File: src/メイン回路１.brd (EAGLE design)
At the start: 22 parts

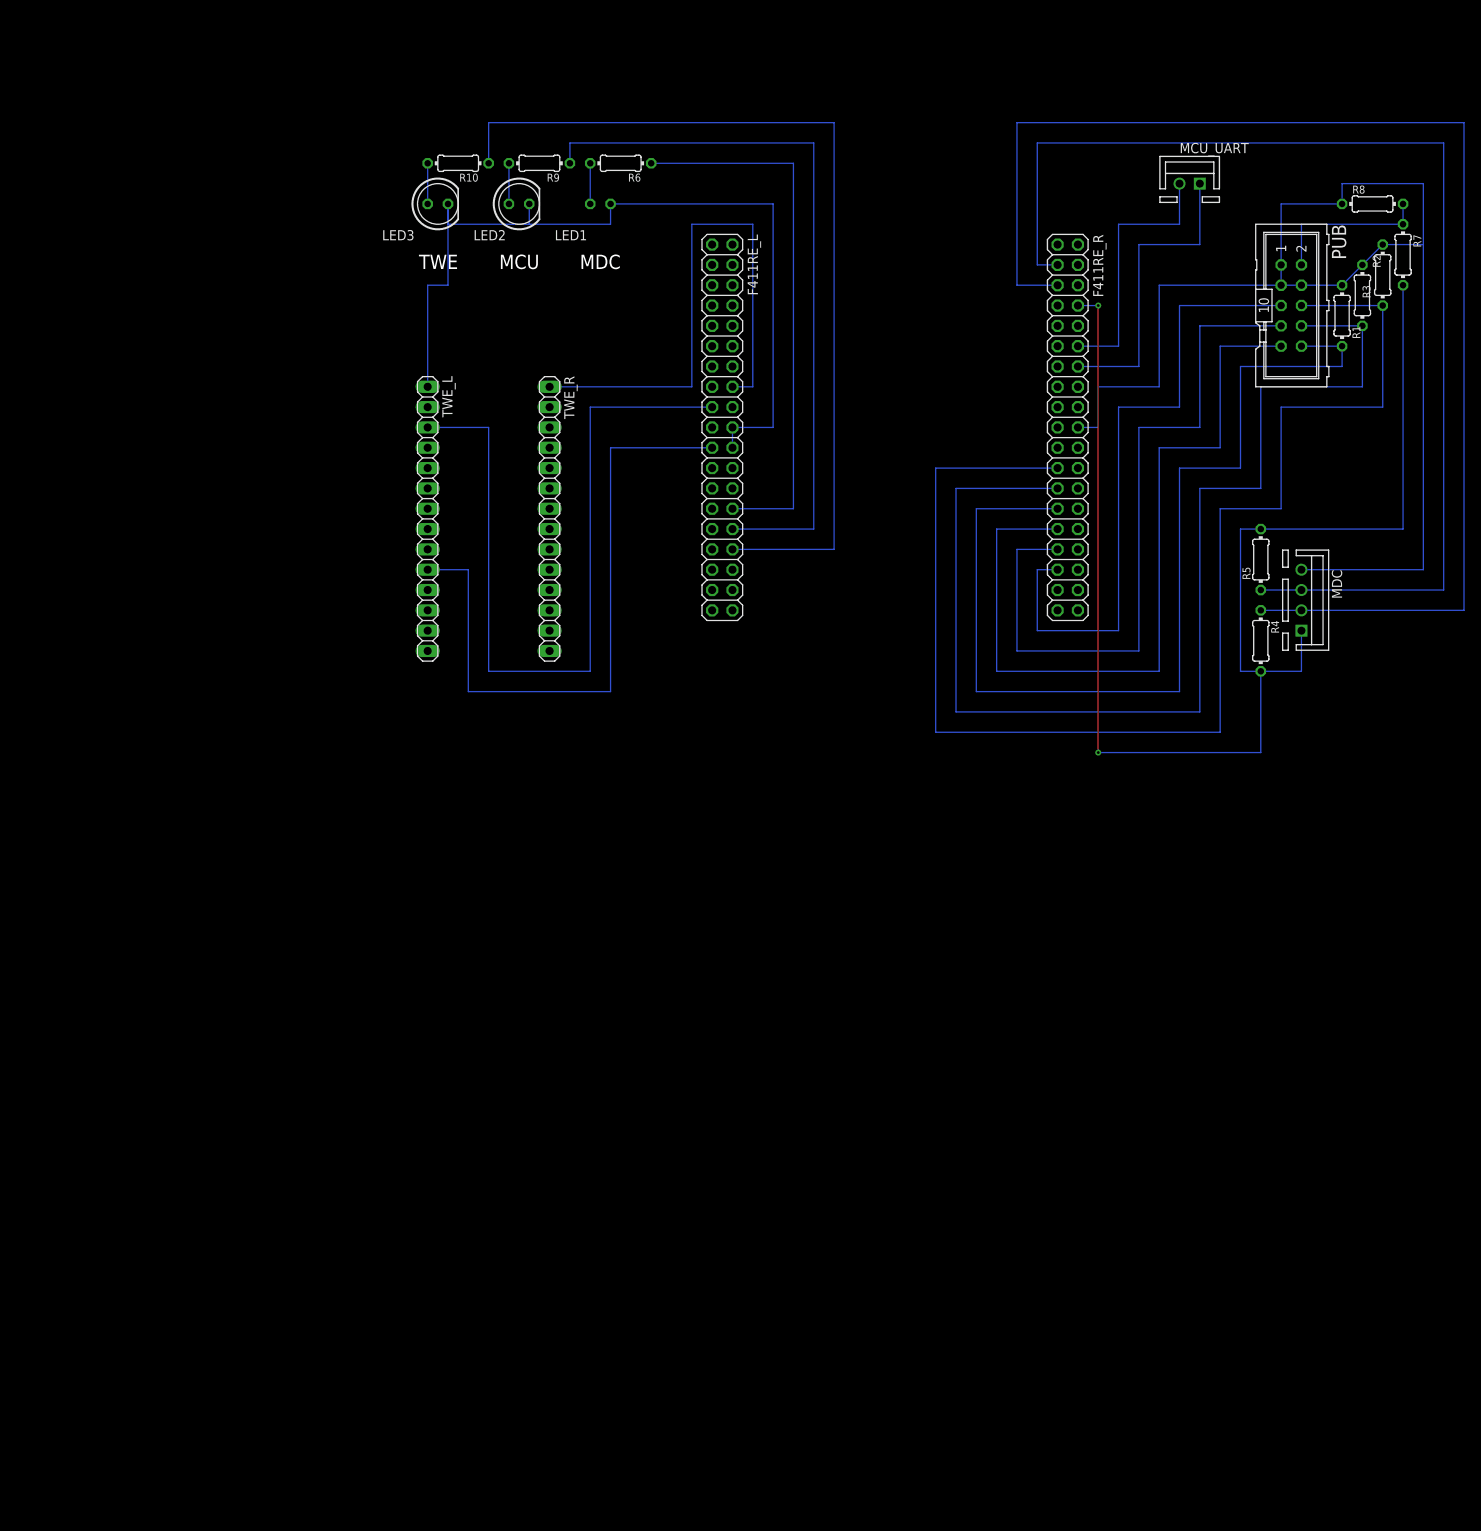
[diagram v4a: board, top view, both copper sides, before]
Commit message: [add]暴走対策回路の追加--ここから--
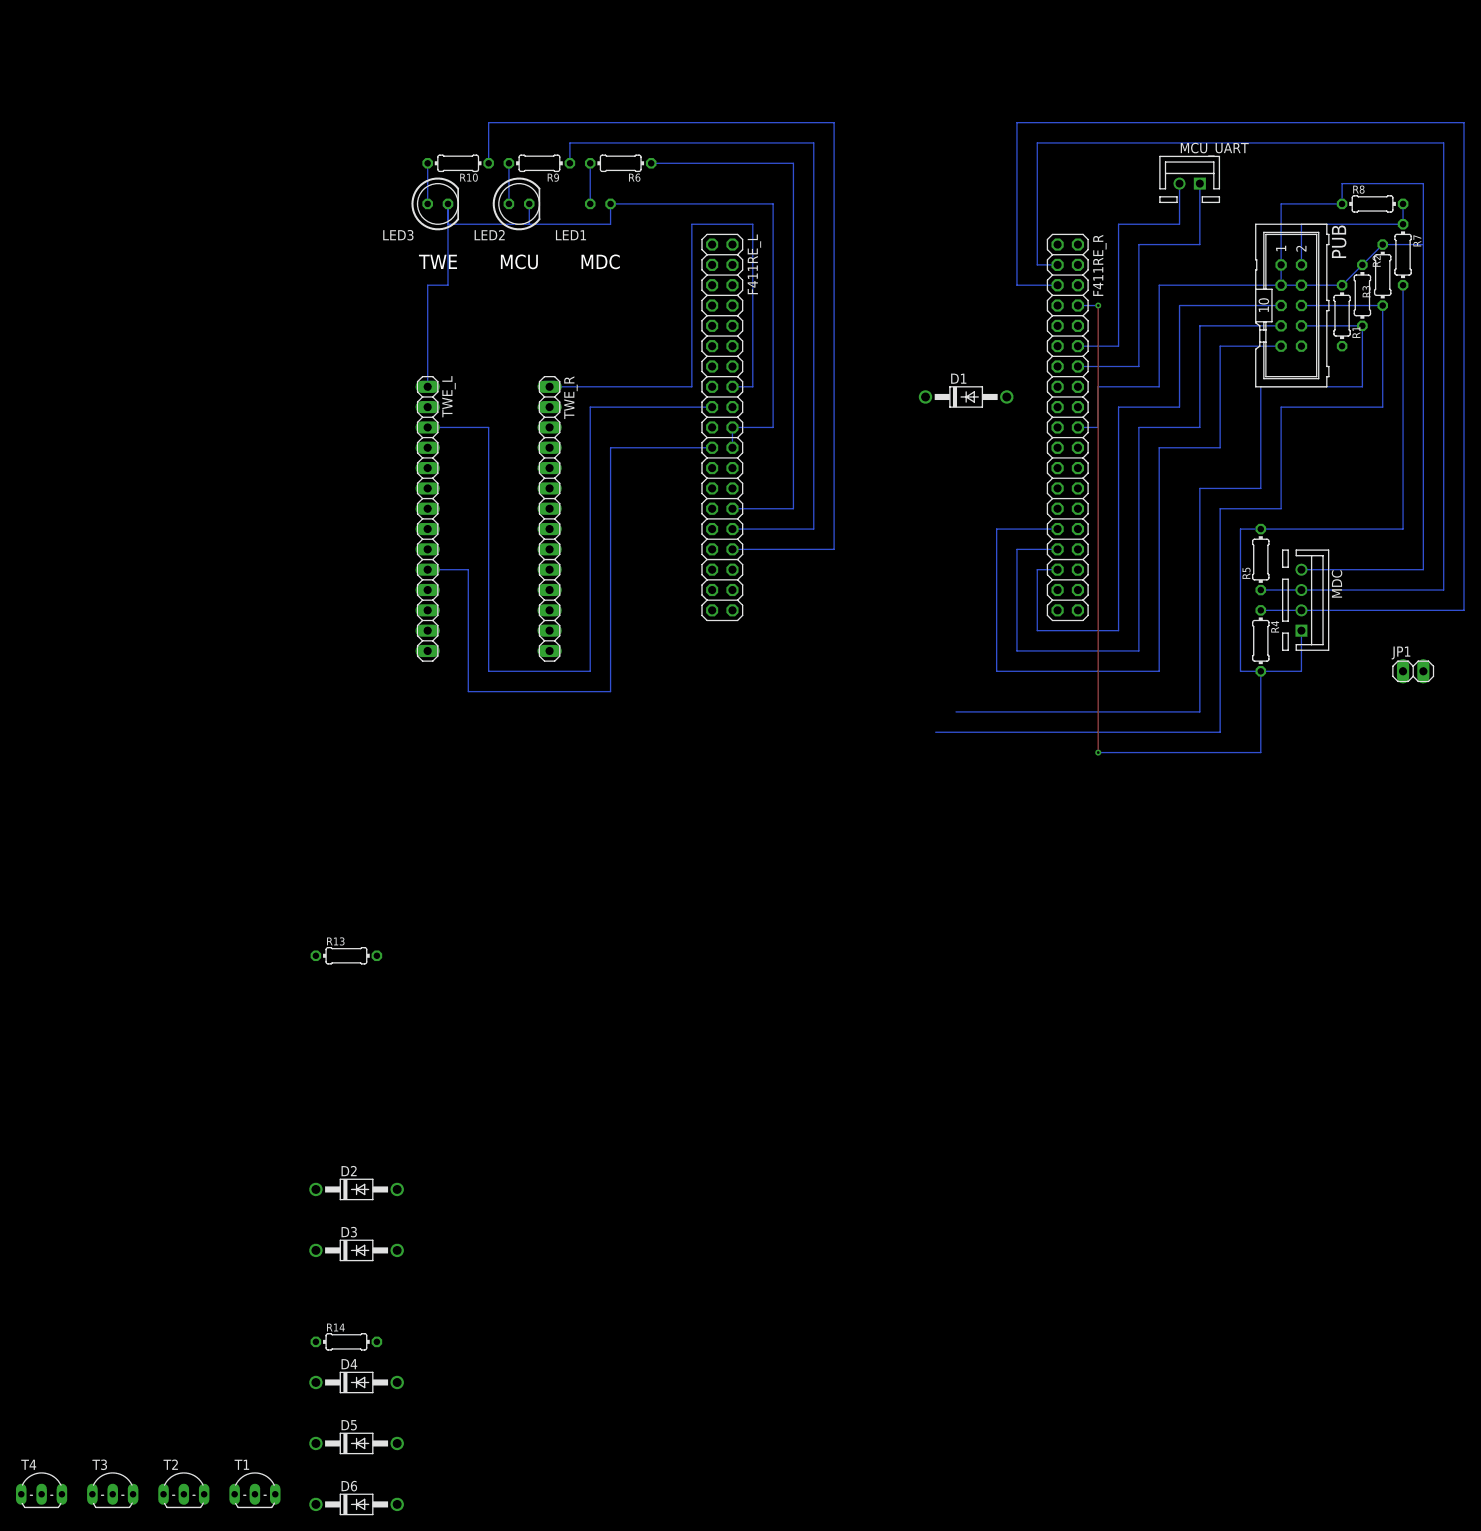
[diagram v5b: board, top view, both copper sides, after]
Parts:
- added D1, D2, D3, D4, D5, D6: 1N4004, diode:DO41-10
- added JP1: (no value), pinhead:1X02
- added R13, R14: 10k, rcl:0204/7
- added T1, T2, T3, T4: 一般的なトランジスタ, 一般的なトランジスタ:TO92-CEB
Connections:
- new net DEBUG: D4.A, D5.A, D6.A, JP1.2, R13.1
- new net N$4: R13.2, T1.B
- new net N$5: D3.C, T2.C
- new net N$6: D2.C, T3.C
- new net N$7: D1.C, T4.C
- new net ZM: R14.1, T1.C, T2.B, T3.B, T4.B
- net DIR1: now also D4.C
- net DIR2: now also D5.C
- net DIR3: now also D6.C
- net GND: now also T1.E
- net PWM1: now also D1.A, T4.E
- net PWM2: now also D2.A, T3.E
- net PWM3: now also D3.A, T2.E
- net U5V: now also JP1.1, R14.2
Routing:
- net PWM1: track 127.0 -> 0.00 mm
- net PWM3: track 167.6 -> 119.4 mm
- net PWM2: track 147.3 -> 106.7 mm

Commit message: [complete]メイン回路1の暴走対策回路の配線完了
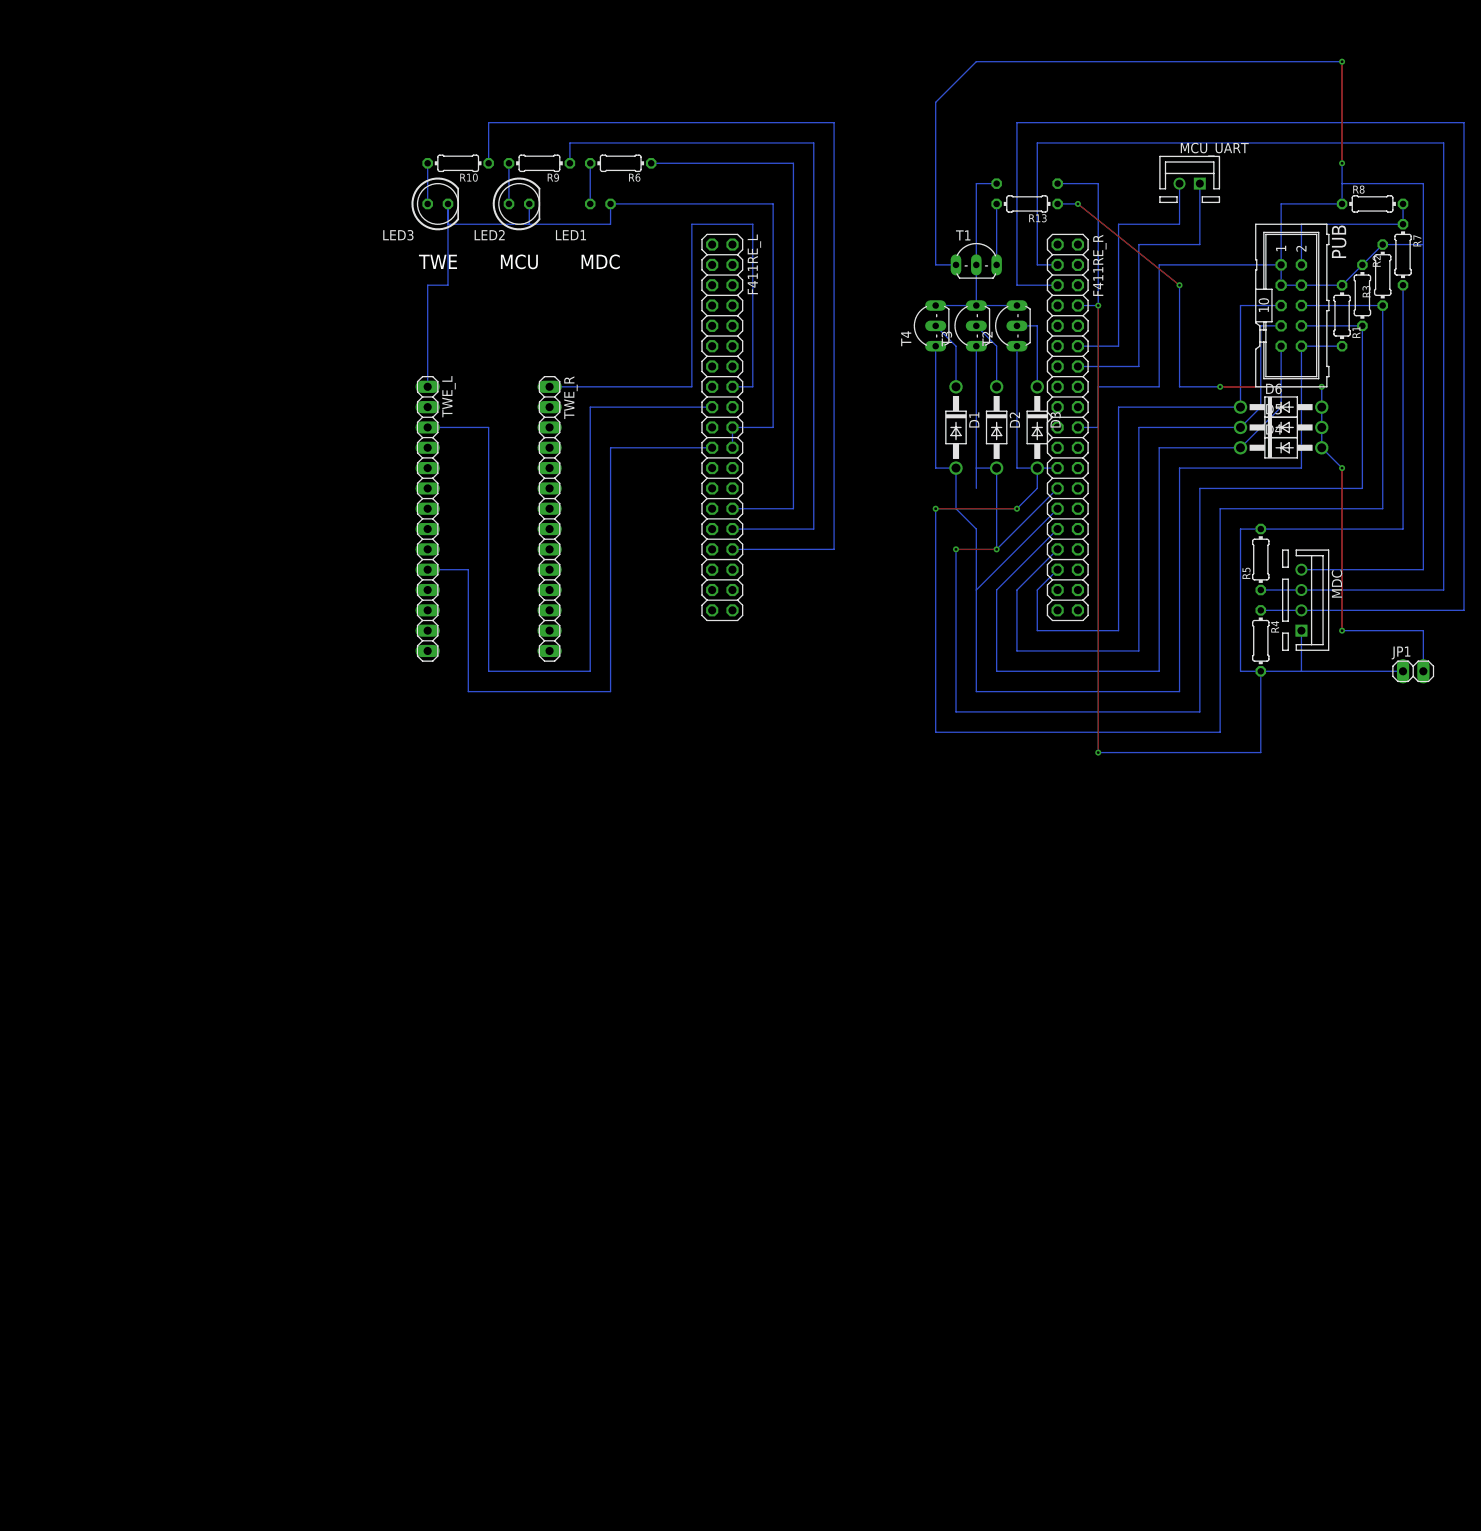
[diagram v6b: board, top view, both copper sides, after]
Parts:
- moved T4 183.9 mm to (63.5, 43.2), turned to 90 degrees
- moved T3 181.6 mm to (68.6, 43.2), turned to 90 degrees
- moved T2 179.4 mm to (73.7, 43.2), turned to 90 degrees
- moved D6 179.4 mm to (106.7, 33.0)
- moved T1 178.2 mm to (68.6, 50.8)
- moved D5 171.7 mm to (106.7, 30.5)
- moved R14 167.9 mm to (74.9, 61.0), flipped to the bottom, turned to 180 degrees
- moved D4 164.3 mm to (106.7, 27.9)
- moved D3 133.5 mm to (76.2, 30.5), turned to 270 degrees
- moved R13 126.8 mm to (74.9, 58.4), turned to 180 degrees
- moved D2 124.4 mm to (71.1, 30.5), turned to 270 degrees
- moved D1 4.02 mm to (66.0, 30.5), turned to 270 degrees
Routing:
- net PWM1: track 0.00 -> 150.0 mm
- net DEBUG: track 0.00 -> 96.1 mm, vias 0 -> 6
- net GND: track 266.3 -> 359.8 mm, vias 0 -> 2
- net PWM2: track 106.7 -> 173.3 mm, vias 0 -> 2
- net PWM3: track 119.4 -> 183.9 mm, vias 0 -> 2
- net U5V: track 170.2 -> 203.2 mm
- net ZM: track 0.00 -> 27.9 mm
- net N$5: track 0.00 -> 10.2 mm
- net N$7: track 0.00 -> 8.67 mm
- net N$6: track 0.00 -> 8.67 mm
- net N$4: track 0.00 -> 7.62 mm
- net DIR1: track 101.6 -> 94.2 mm
- net DIR2: track 91.4 -> 87.0 mm
- net DIR3: track 81.3 -> 79.8 mm
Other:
- board text added: "⇐MILコネクタ付ける前に配線すること!!"
